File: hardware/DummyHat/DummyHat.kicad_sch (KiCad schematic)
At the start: 1 part, among them U1 7404

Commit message: Finish First Dummy Hat Design
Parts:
- removed U1: 7404, 7404:N14, symbol 74xx_IEEE:7404
- added D1, D2, D3, D4, D5: D, Diode_THT:D_DO-34_SOD68_P7.62mm_Horizontal, symbol Device:D
- added D6, D7, D8, D9: LED, LED_THT:LED_D5.0mm, symbol Device:LED
- added J1, J2, J3: Conn_01x08_Socket, Connector_PinSocket_2.54mm:PinSocket_1x08_P2.54mm_Vertical, symbol Connector:Conn_01x08_Socket
- added R1, R2, R3, R4: R, Resistor_THT:R_Axial_DIN0207_L6.3mm_D2.5mm_P10.16mm_Horizontal, symbol Device:R
- added U1: 74HC04, 7404:N14, symbol 74xx:74HC04
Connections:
- net +5V: now also J1.8 (Pin_8), U1.14 (VCC)
- net GND: now also J1.1 (Pin_1), R1.2, R2.2, R3.2, R4.2, U1.11, U1.3, U1.5, U1.7 (GND), U1.9
- new net: D1.1 (K), D2.1 (K), D3.1 (K), D4.1 (K), D5.1 (K), U1.13
- new net: D6.1 (K), R1.1
- new net: D7.1 (K), R2.1
- new net: D8.1 (K), R3.1
- new net: D9.1 (K), R4.1
- new net: D1.2 (A), U1.2
- new net D0: D6.2 (A), J2.1 (Pin_1)
- new net D1: D7.2 (A), J2.2 (Pin_2)
- new net D10: J3.3 (Pin_3)
- new net D11: J3.4 (Pin_4)
- new net D12: J3.5 (Pin_5)
- new net D13: J3.6 (Pin_6)
- new net D14: J3.7 (Pin_7)
- new net D15: J3.8 (Pin_8)
- new net D2: D8.2 (A), J2.3 (Pin_3)
- new net D3: D9.2 (A), J2.4 (Pin_4)
- new net D4: J2.5 (Pin_5)
- new net D5: J2.6 (Pin_6)
- new net D6: J2.7 (Pin_7)
- new net D7: J2.8 (Pin_8)
- new net D8: J3.1 (Pin_1)
- new net D9: J3.2 (Pin_2)
- new net I0: J1.2 (Pin_2), U1.1
- new net I1: D2.2 (A), J1.3 (Pin_3)
- new net I2: D3.2 (A), J1.4 (Pin_4)
- new net I3: D4.2 (A), J1.5 (Pin_5)
- new net I4: D5.2 (A), J1.6 (Pin_6)
- new net RESP: J1.7 (Pin_7), U1.12
- no-connect marks 0 -> 4
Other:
- note added: "Value: 00001"

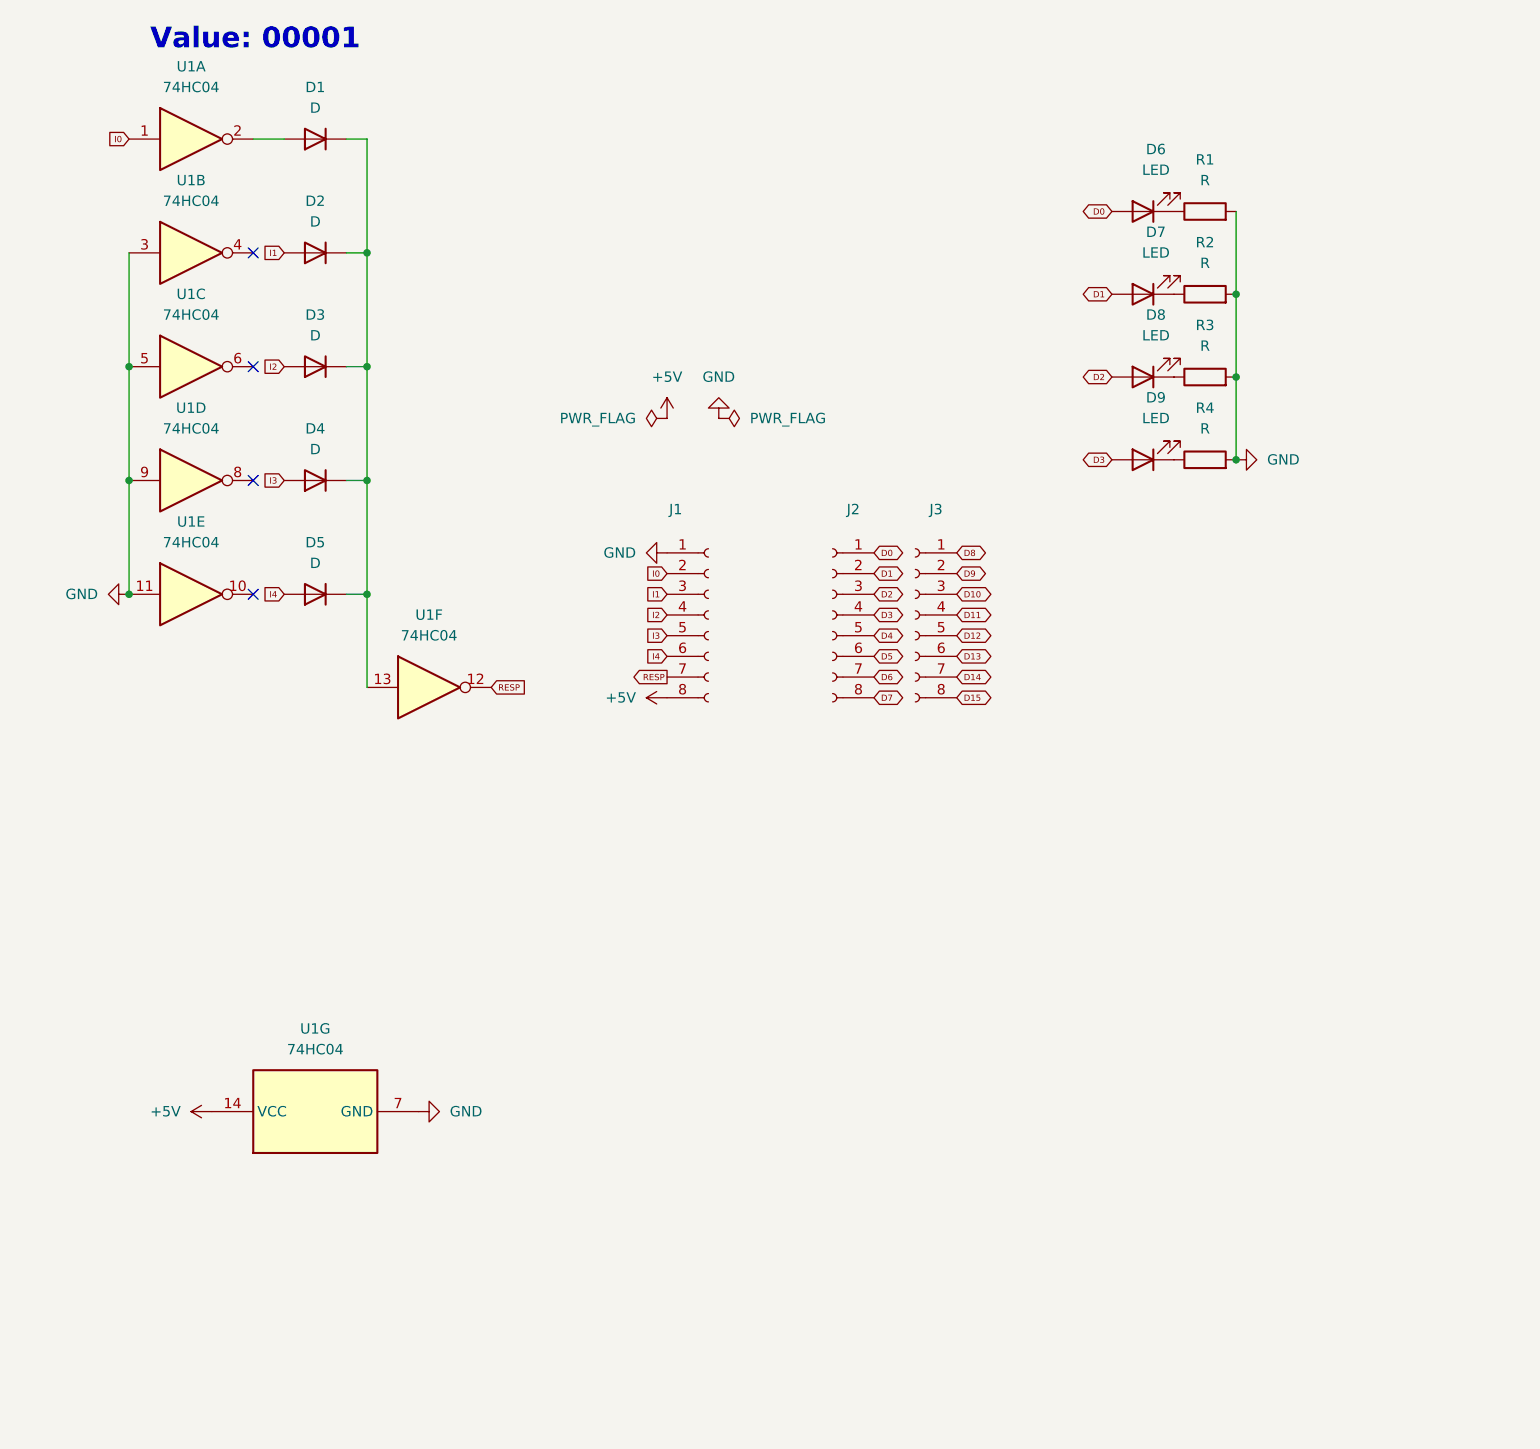
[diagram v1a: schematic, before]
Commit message: Update dummy board schematic
Update dummy board schematic to use octal tranciever chip. Issues. Data pins are now one way and do not support analog.
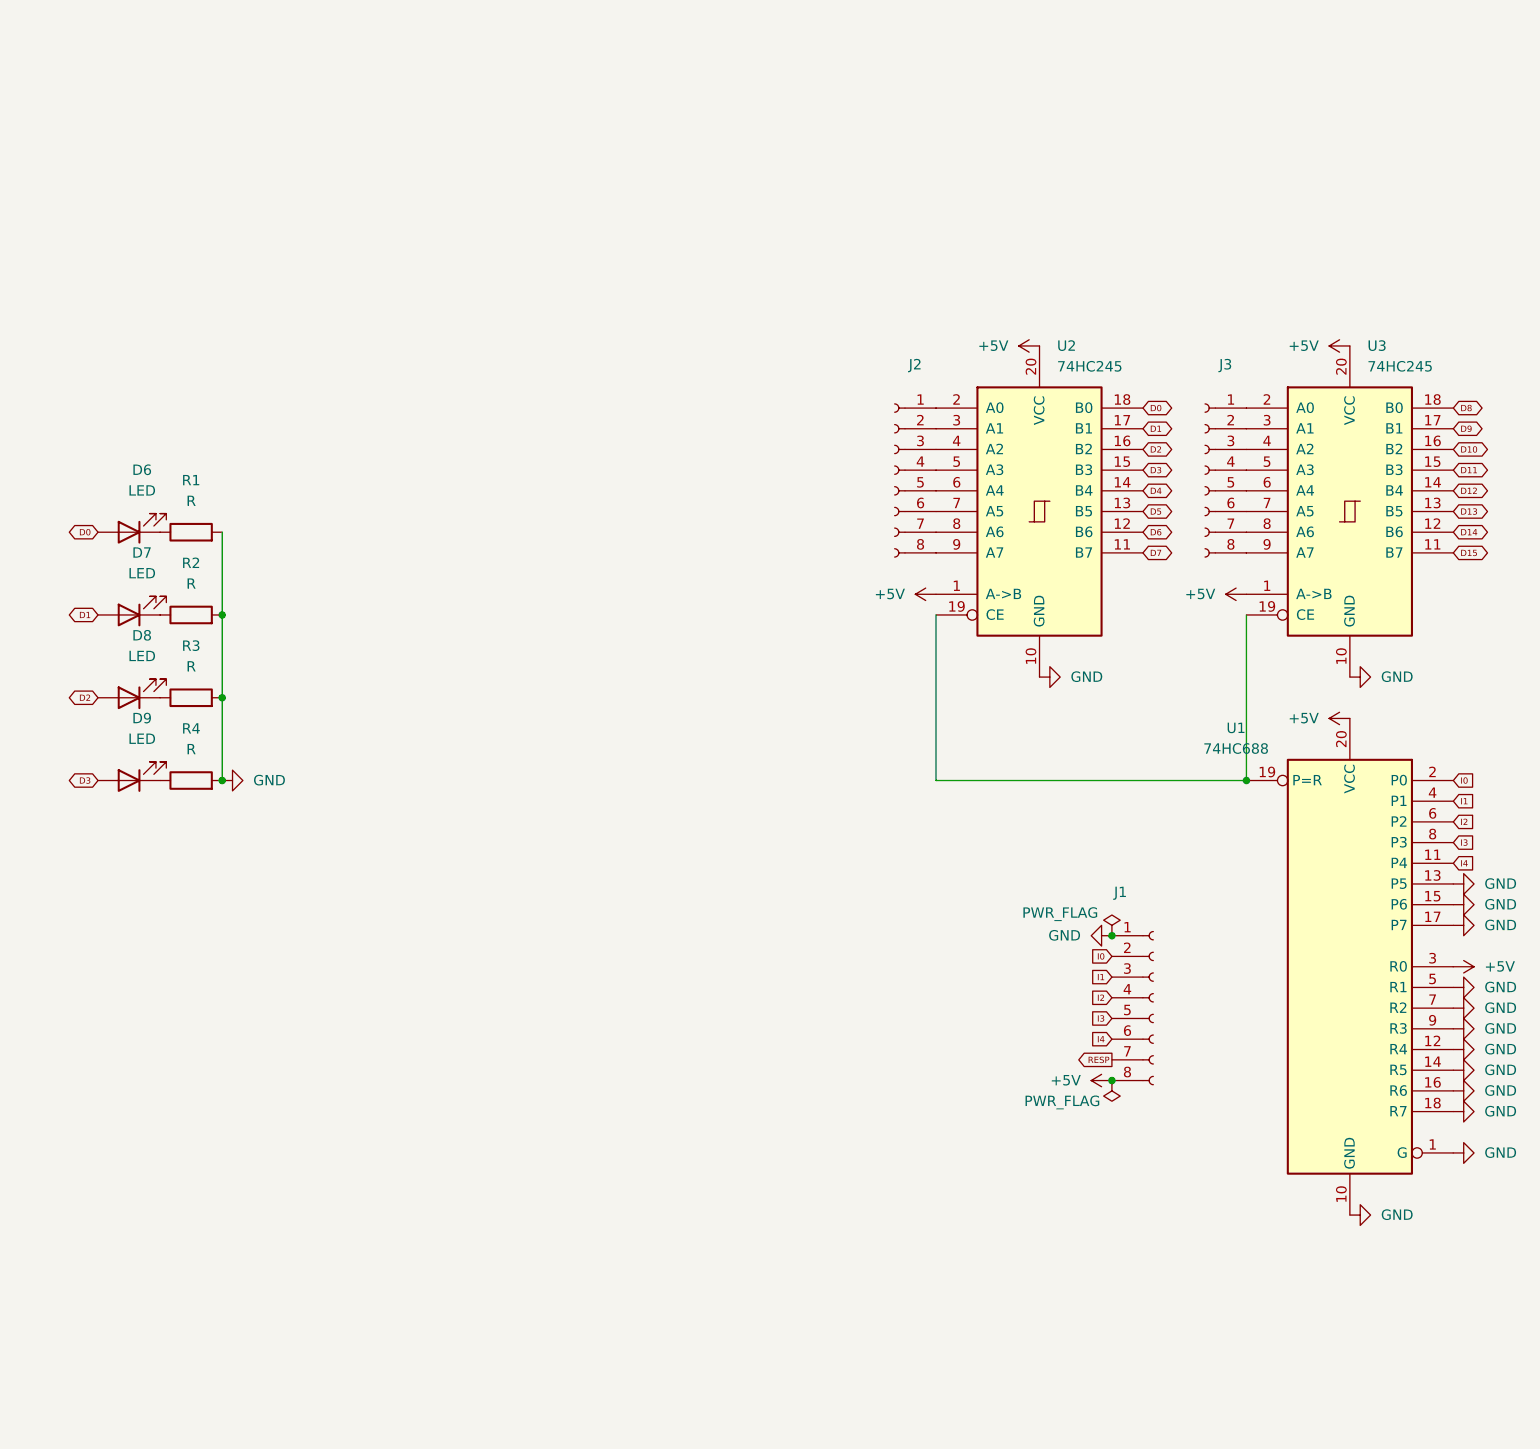
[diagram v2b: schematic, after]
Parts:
- removed D1, D2, D3, D4, D5: D, Diode_THT:D_DO-34_SOD68_P7.62mm_Horizontal, symbol Device:D
- removed U1: 74HC04, 7404:N14, symbol 74xx:74HC04
- added U1: 74HC688, symbol 74xx:74HC688
- added U2, U3: 74HC245, symbol 74xx:74HC245
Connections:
- net +5V: now also U1.20 (VCC), U1.3 (R0), U2.1 (A->B), U2.20 (VCC), U3.1 (A->B), U3.20 (VCC)
- net D0: now also U2.18 (B0); no longer J2.1 (Pin_1)
- net D1: now also U2.17 (B1); no longer J2.2 (Pin_2)
- net D10: now also U3.16 (B2); no longer J3.3 (Pin_3)
- net D11: now also U3.15 (B3); no longer J3.4 (Pin_4)
- net D12: now also U3.14 (B4); no longer J3.5 (Pin_5)
- net D13: now also U3.13 (B5); no longer J3.6 (Pin_6)
- net D14: now also U3.12 (B6); no longer J3.7 (Pin_7)
- net D15: now also U3.11 (B7); no longer J3.8 (Pin_8)
- net D2: now also U2.16 (B2); no longer J2.3 (Pin_3)
- net D3: now also U2.15 (B3); no longer J2.4 (Pin_4)
- net D4: now also U2.14 (B4); no longer J2.5 (Pin_5)
- net D5: now also U2.13 (B5); no longer J2.6 (Pin_6)
- net D6: now also U2.12 (B6); no longer J2.7 (Pin_7)
- net D7: now also U2.11 (B7); no longer J2.8 (Pin_8)
- net D8: now also U3.18 (B0); no longer J3.1 (Pin_1)
- net D9: now also U3.17 (B1); no longer J3.2 (Pin_2)
- net GND: now also U1.1 (G), U1.10 (GND), U1.12 (R4), U1.13 (P5), U1.14 (R5), U1.15 (P6), U1.16 (R6), U1.17 (P7), U1.18 (R7), U1.5 (R1), U1.7 (R2), U1.9 (R3), U2.10 (GND), U3.10 (GND)
- net I0: now also U1.2 (P0)
- net I1: now also U1.4 (P1)
- net I2: now also U1.6 (P2)
- net I3: now also U1.8 (P3)
- net I4: now also U1.11 (P4)
- new net: J2.1 (Pin_1), U2.2 (A0)
- new net: J2.2 (Pin_2), U2.3 (A1)
- new net: J2.3 (Pin_3), U2.4 (A2)
- new net: J2.4 (Pin_4), U2.5 (A3)
- new net: J2.5 (Pin_5), U2.6 (A4)
- new net: J2.6 (Pin_6), U2.7 (A5)
- new net: J2.7 (Pin_7), U2.8 (A6)
- new net: J2.8 (Pin_8), U2.9 (A7)
- new net: U1.19 (P=R), U2.19 (CE), U3.19 (CE)
- new net: J3.1 (Pin_1), U3.2 (A0)
- new net: J3.2 (Pin_2), U3.3 (A1)
- new net: J3.3 (Pin_3), U3.4 (A2)
- new net: J3.4 (Pin_4), U3.5 (A3)
- new net: J3.5 (Pin_5), U3.6 (A4)
- new net: J3.6 (Pin_6), U3.7 (A5)
- new net: J3.7 (Pin_7), U3.8 (A6)
- new net: J3.8 (Pin_8), U3.9 (A7)
- no-connect marks 4 -> 0
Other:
- note removed: "Value: 00001"
- moved on the sheet: D6, D7, D8, D9, J1, J2, J3, R1, R2, R3, R4

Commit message: Finish dev board. Limitations still apply.
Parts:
- added D1, D10, D11, D12, D13, D14, D15, D2, D3, D4, D5: LED, LED_THT:LED_D5.0mm, symbol Device:LED
- added R10, R11, R12, R13, R14, R15, R5, R6, R7, R8, R9: R, Resistor_THT:R_Axial_DIN0207_L6.3mm_D2.5mm_P10.16mm_Horizontal, symbol Device:R
- U1, U2, U3: footprint (none) -> Package_DIP:DIP-20_W7.62mm
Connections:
- net D15 is gone; now on net D14: U3.11 (B7)
- net +5V: now also U2.2 (A0)
- net D0: now also U2.17 (B1); no longer U2.18 (B0)
- net D1: now also U2.16 (B2); no longer U2.17 (B1)
- net D10: now also U3.15 (B3), D11.2 (A); no longer U3.16 (B2)
- net D11: now also U3.14 (B4), D12.2 (A); no longer U3.15 (B3)
- net D12: now also U3.13 (B5), D13.2 (A); no longer U3.14 (B4)
- net D13: now also U3.12 (B6), D14.2 (A); no longer U3.13 (B5)
- net D14: now also D15.2 (A); no longer U3.12 (B6)
- net D2: now also U2.15 (B3); no longer U2.16 (B2)
- net D3: now also U2.14 (B4); no longer U2.15 (B3)
- net D4: now also U2.13 (B5), D1.2 (A); no longer U2.14 (B4)
- net D5: now also U2.12 (B6), D2.2 (A); no longer U2.13 (B5)
- net D6: now also U2.11 (B7), D3.2 (A); no longer U2.12 (B6)
- net D7: now also U3.18 (B0), D4.2 (A); no longer U2.11 (B7)
- net D8: now also U3.17 (B1), D5.2 (A); no longer U3.18 (B0)
- net D9: now also U3.16 (B2), D10.2 (A); no longer U3.17 (B1)
- net GND: now also R10.2, R11.2, R12.2, R13.2, R14.2, R15.2, R5.2, R6.2, R7.2, R8.2, R9.2; no longer U1.13 (P5)
- net at J2.1 (Pin_1): now also U2.18 (B0); no longer U2.2 (A0)
- net RESP renamed I5
- net I5: now also U1.13 (P5)
- new net: D11.1 (K), R11.1
- new net: D15.1 (K), R15.1
- new net: D12.1 (K), R12.1
- new net: D10.1 (K), R10.1
- new net: D13.1 (K), R13.1
- new net: D2.1 (K), R6.1
- new net: D1.1 (K), R5.1
- new net: D5.1 (K), R9.1
- new net: D14.1 (K), R14.1
- new net: D3.1 (K), R7.1
- new net: D4.1 (K), R8.1
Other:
- moved on the sheet: J2

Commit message: add not gate to dummy board for 16 data pins
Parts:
- added Q1: PN2222A, Package_TO_SOT_THT:TO-92_Inline, symbol Transistor_BJT:PN2222A
- added R1, R2: 1k, Resistor_THT:R_Axial_DIN0207_L6.3mm_D2.5mm_P10.16mm_Horizontal, symbol Device:R
- renumbered R1 to R16, R2 to R17
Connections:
- net +5V: now also R1.1; no longer U2.2 (A0)
- net D0: now also U2.18 (B0); no longer D6.2 (A), U2.17 (B1)
- net D1: now also D6.2 (A), U2.17 (B1); no longer D7.2 (A), U2.16 (B2)
- net D10: now also D10.2 (A), U3.16 (B2); no longer D11.2 (A), U3.15 (B3)
- net D11: now also D11.2 (A), U3.15 (B3); no longer D12.2 (A), U3.14 (B4)
- net D12: now also D12.2 (A), U3.14 (B4); no longer D13.2 (A), U3.13 (B5)
- net D13: now also D13.2 (A), U3.13 (B5); no longer D14.2 (A), U3.12 (B6)
- net D14: now also D14.2 (A), U3.12 (B6); no longer D15.2 (A), U3.11 (B7)
- net D2: now also D7.2 (A), U2.16 (B2); no longer D8.2 (A), U2.15 (B3)
- net D3: now also D8.2 (A), U2.15 (B3); no longer D9.2 (A), U2.14 (B4)
- net D4: now also D9.2 (A), U2.14 (B4); no longer D1.2 (A), U2.13 (B5)
- net D5: now also D1.2 (A), U2.13 (B5); no longer D2.2 (A), U2.12 (B6)
- net D6: now also D2.2 (A), U2.12 (B6); no longer D3.2 (A), U2.11 (B7)
- net D7: now also D3.2 (A), U2.11 (B7); no longer D4.2 (A), U3.18 (B0)
- net D8: now also D4.2 (A), U3.18 (B0); no longer D5.2 (A), U3.17 (B1)
- net D9: now also D5.2 (A), U3.17 (B1); no longer D10.2 (A), U3.16 (B2)
- net GND: now also U1.13 (P5), Q1.1 (E)
- net at J2.1 (Pin_1): now also U2.2 (A0); no longer U2.18 (B0)
- net at U1.19 (P=R), U2.19 (CE), U3.19 (CE): now also R2.1
- net I5 renamed RESP
- net RESP: now also Q1.3 (C), R1.2; no longer U1.13 (P5)
- new net: Q1.2 (B), R2.2
- new net D15: D15.2 (A), U3.11 (B7)
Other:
- moved on the sheet: J1, J2
